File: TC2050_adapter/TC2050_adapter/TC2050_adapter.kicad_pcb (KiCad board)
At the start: 2 copper layers, 76.7 x 15.2 mm, 10 parts, among them J1 Conn_01x05, J11 TC2050_pogo, J2 Cortex Debug 10-pin connector, J3 Conn_01x05, J4 Conn_01x05, J5 TC2050_pogo, J6 Conn_01x05, J7 TC2050_pogo_alignment, J8 TC2050_pogo, J9 TC2050_pogo

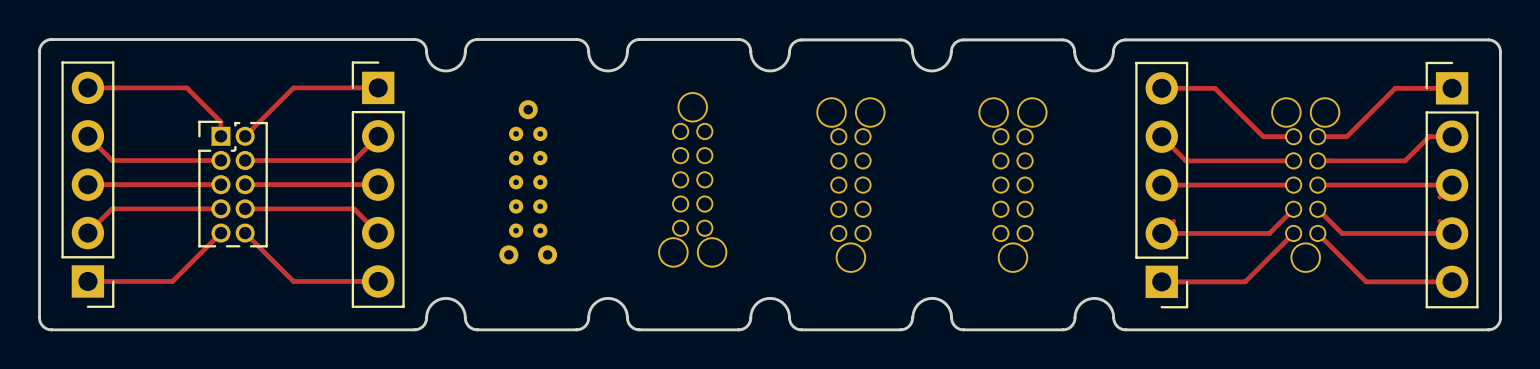
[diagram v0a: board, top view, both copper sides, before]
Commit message: adding testing jigs
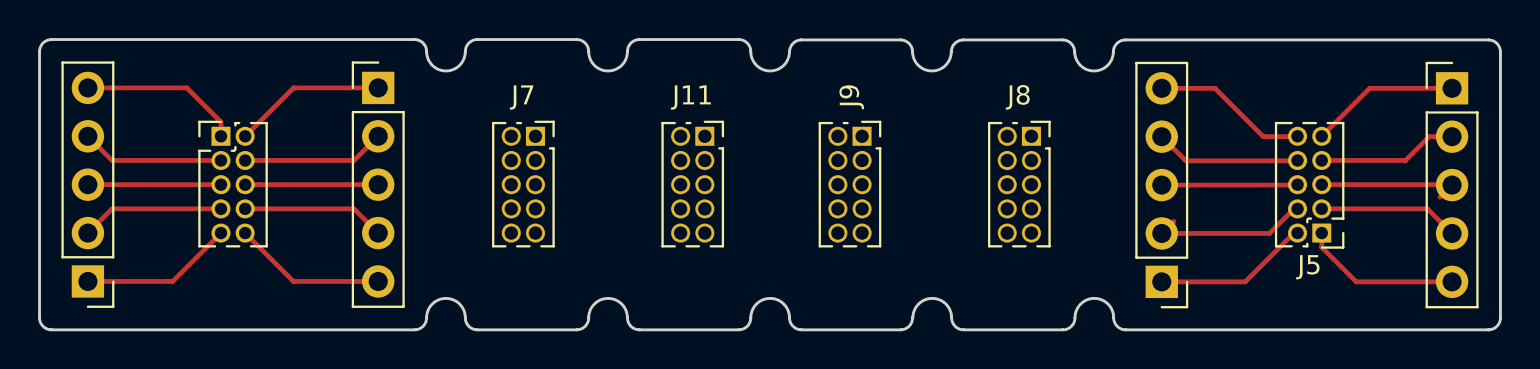
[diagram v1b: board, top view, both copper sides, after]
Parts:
- J11, J8, J9: footprint E73:TC2050_pogo -> Connector_PinSocket_1.27mm:PinSocket_2x05_P1.27mm_Vertical
- J5: value TC2050_pogo -> Cortex Debug 10-pin connector; footprint E73:TC2050_pogo -> Connector_PinHeader_1.27mm:PinHeader_2x05_P1.27mm_Vertical
- J7: footprint E73:TC2050_alignment -> Connector_PinSocket_1.27mm:PinSocket_2x05_P1.27mm_Vertical
- moved J8 2.74 mm to (77.5, 30.5), turned to 0 degrees
- moved J5 2.66 mm to (92.7, 35.6)
- moved J9 2.63 mm to (68.6, 30.5), turned to 0 degrees
- moved J7 2.44 mm to (51.4, 30.5)
- moved J11 2.37 mm to (60.3, 30.5)
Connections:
- J5 pad 2: Net-(J4-Pad4) -> Net-(J5-Pad2)
- J5 pad 3: Net-(J4-Pad3) -> Net-(J4-Pad4)
- J5 pad 4: Net-(J4-Pad2) -> Net-(J5-Pad4)
- J5 pad 5: Net-(J4-Pad1) -> Net-(J4-Pad3)
- J5 pad 7: Net-(J5-Pad7) -> Net-(J4-Pad2)
- J5 pad 9: Net-(J5-Pad9) -> Net-(J4-Pad1)
- J6 pad 1: Net-(J5-Pad10) -> Net-(J5-Pad2)
- J6 pad 2: Net-(J5-Pad9) -> Net-(J5-Pad4)
- J6 pad 3: Net-(J5-Pad8) -> Net-(J5-Pad6)
- J6 pad 4: Net-(J5-Pad7) -> Net-(J5-Pad8)
- J6 pad 5: Net-(J5-Pad6) -> Net-(J5-Pad10)
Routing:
- net Net-(J5-Pad9): track 8.35 -> 0.00 mm
- net Net-(J5-Pad4): track 0.00 -> 8.35 mm
- net Net-(J5-Pad2): track 0.00 -> 7.97 mm
- net Net-(J5-Pad7): track 7.45 -> 0.00 mm
- net Net-(J5-Pad6): track 7.97 -> 6.92 mm
- net Net-(J5-Pad8): track 6.92 -> 7.45 mm
